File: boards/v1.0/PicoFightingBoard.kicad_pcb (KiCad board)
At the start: 2 copper layers, 96.1 x 45.2 mm, 25 parts, among them J5 Screw_Terminal_01x05, J6 Screw_Terminal_01x05, J7 Screw_Terminal_01x05, J8 Screw_Terminal_01x05, U1 Pico, U2 SN74LV1T34DBV

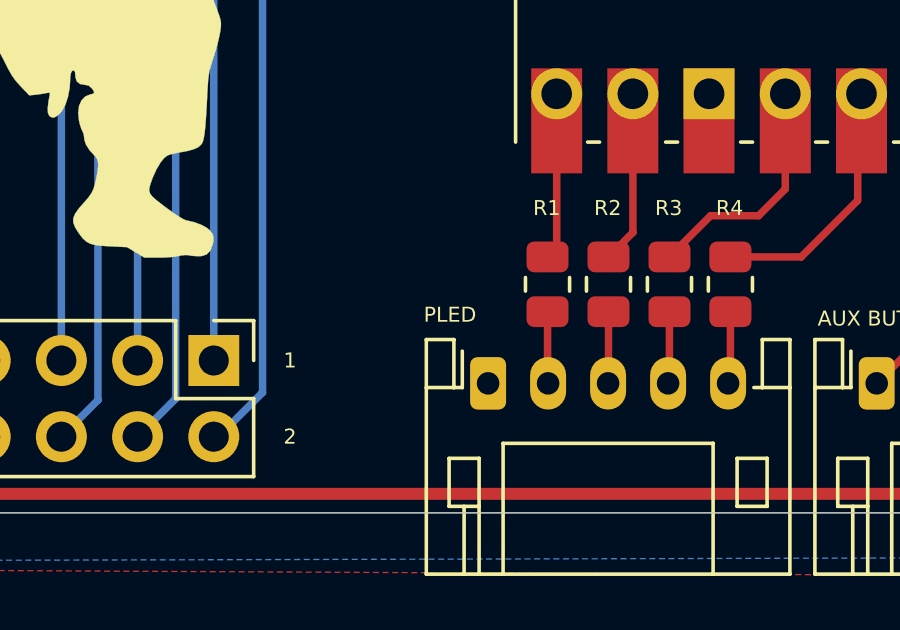
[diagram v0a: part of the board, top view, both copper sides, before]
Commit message: Fix pin 12 ground on 20-pin connector
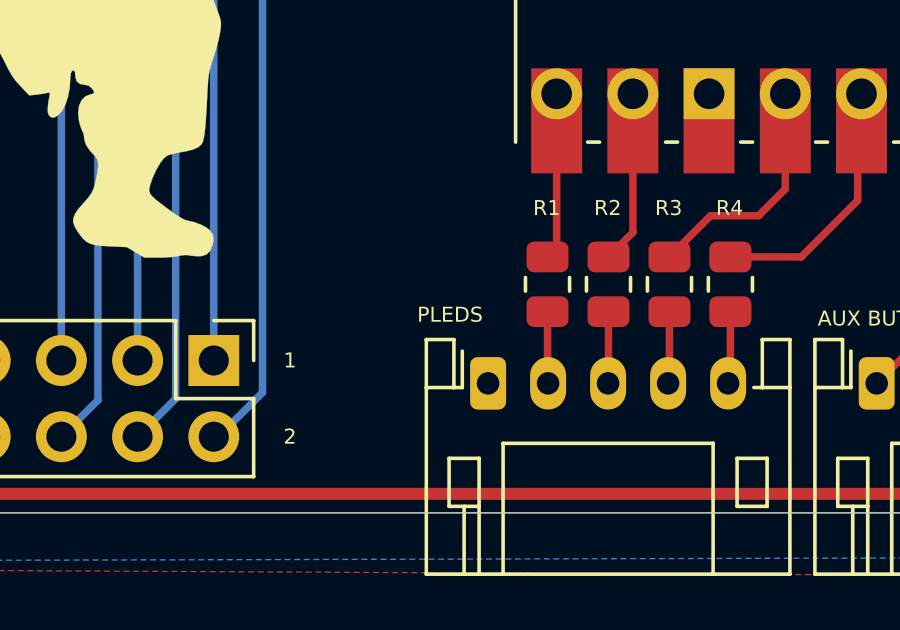
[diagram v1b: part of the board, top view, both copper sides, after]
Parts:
- renumbered PLED to PLEDS
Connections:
- 20-PIN HARNESS pad 12: (no net) -> /GND
- U2 pad 1: (no net) -> Net-(U2-Pad1)
